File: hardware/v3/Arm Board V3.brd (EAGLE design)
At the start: 165.1 x 76.2 mm, 80 parts, among them CN1 1X4-BIG, IC1 L6206D, IC2 L6206D, IC3 L6206D, IC4 7812TV, IC5 7812TV, IC6 7812TV, IC7 7812DT, IC9 7812DT, Q1 Q_LTC490, Q3 Q_LTC490, U1 MAX3468CPA, U2 XBEE-1B3

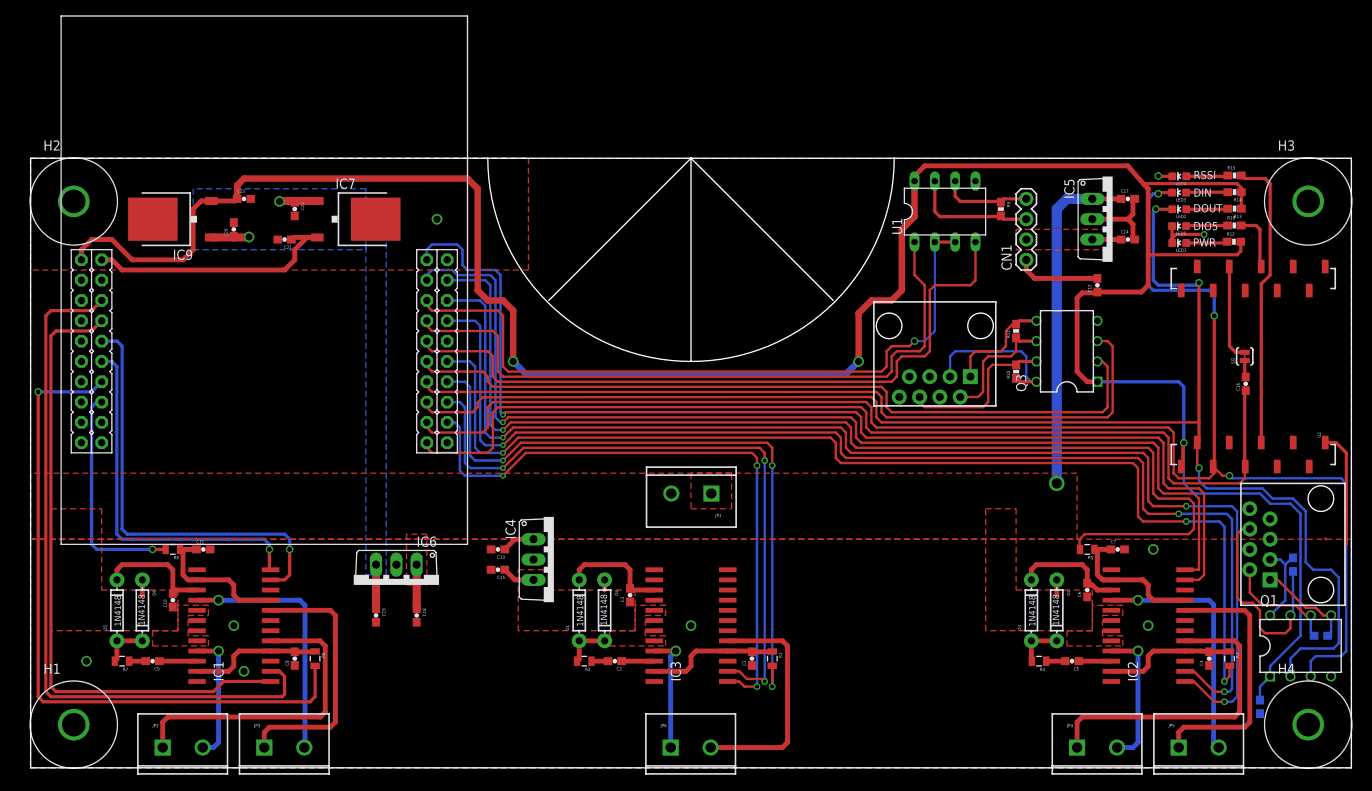
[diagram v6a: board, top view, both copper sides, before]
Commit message: Added headers for serial in and 2 encoders
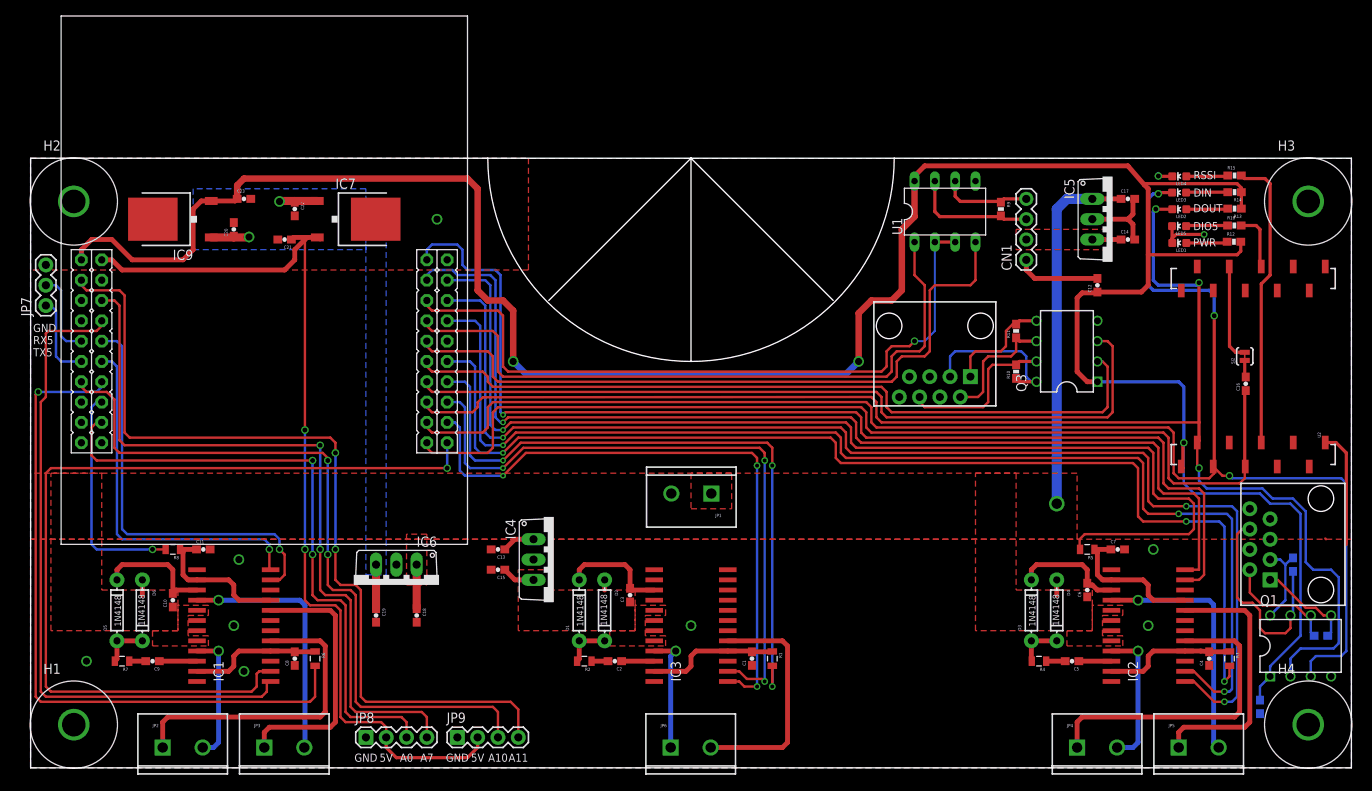
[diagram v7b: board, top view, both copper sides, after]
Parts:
- added JP7: (no value), SparkFun-Connectors:1X03
- added JP8, JP9: (no value), SparkFun-Connectors:1X04
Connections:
- new net A0: JP8.3, U$1.PE3
- new net A10: JP9.3, U$1.PB4
- new net A11: JP9.4, U$1.PB5
- new net A7: JP8.4, U$1.PD0
- new net RXD5: JP7.2, U$1.PE4
- new net TXD5: JP7.1, U$1.PE5
- net +5V: now also JP8.2, JP9.2
- net GND: now also JP7.3, JP8.1, JP9.1
- net IN2_A_1: now also U$1.PA2; no longer U$1.PD0
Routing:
- net A11: track 0.00 -> 108.6 mm, vias 0 -> 2
- net A10: track 0.00 -> 93.4 mm, vias 0 -> 2
- net A7: track 0.00 -> 93.0 mm, vias 0 -> 2
- net +5V: track 32.0 -> 118.4 mm, vias 0 -> 2
- net A0: track 0.00 -> 77.8 mm, vias 0 -> 2
- net IN2_A_1: track 89.2 -> 110.6 mm, vias 0 -> 1
- net TXD5: track 0.00 -> 10.7 mm
- net RXD5: track 0.00 -> 10.7 mm
- net IN1_A_1: track 79.2 -> 83.6 mm
- net VIN: track 56.3 -> 58.8 mm
- net IN1_B_1: track 54.2 -> 52.6 mm
- net EN_A_1: track 85.6 -> 86.4 mm
- net GND: vias 9 -> 10
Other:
- board text added: "5V"
- board text added: "A0"
- board text added: "A10"
- board text added: "A11"
- board text added: "A7"
- board text added: "GND"
- board text added: "GND RX5 TX5"

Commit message: Cleaned up and made sure it complied with 4pcb DRU
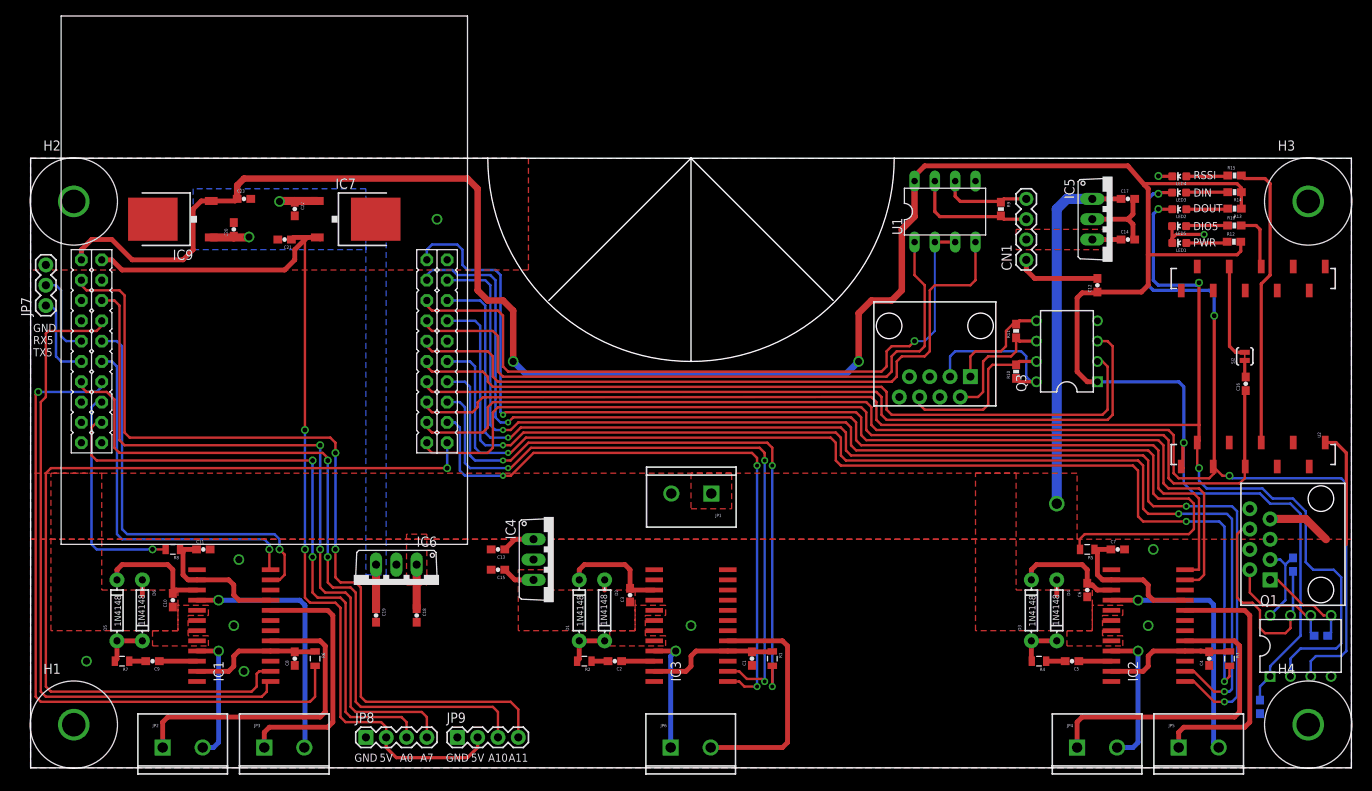
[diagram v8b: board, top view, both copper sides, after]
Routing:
- net GND: track 44.5 -> 52.5 mm
- net RXD3: track 186.6 -> 187.4 mm
- net RXD1: track 96.5 -> 97.1 mm
- net TXD1: track 99.7 -> 100.4 mm
- net B1_1: track 33.0 -> 32.4 mm
- net N$2: track 20.3 -> 20.9 mm
